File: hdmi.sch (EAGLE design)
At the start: 146 parts, among them IC1 FT2232HQ, U0 6SLX45CSG324, U1 MT41J64M16, U2 TPD12S016RKTR, U3 TPD12S016RKTR, U4 TPD12S016RKTR, U5 MNR18, U6 MNR18, U8 20Mhz

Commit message: +Bluetooth module
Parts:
- added C64, C65: 0.1, prj-hdmi:C-EU0402
- added R42, R47: 10k, prj-hdmi:R-EU_0402
- added U$11: PAN1322, prj-hdmi:PAN1322
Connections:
- new net BT_CTS: U$11.P0.7_UARTCTS, U0B2.IO_L63N_2
- new net BT_RESET#: R42.2, U$11.RESET#, U0B2.IO_L48N_RDWR_B_VREF_2
- new net BT_RTS: U$11.P0.6_UARTRTS, U0B2.IO_L63P_2
- new net BT_RX: U$11.P0.5_UARTRXD, U0B2.IO_L62N_D6_2
- new net BT_SCL: U$11.P0.13_SCL0, U0B2.IO_L49N_D4_2
- new net BT_SDA: U$11.P0.12_SDA0, U0B2.IO_L49P_D3_2
- new net BT_TX: U$11.P0.4_UARTTXD, U0B2.IO_L62P_D5_2
- new net BT_WAKE: R47.1, U$11.P0.14_LPMIN, U0B2.IO_L48P_D7_2
- net +3V3: now also C64.1, C65.1, R47.2, U$11.ONOFF, U$11.VDD1, U$11.VDDUART, U$11.VSUPPLY@A4, U$11.VSUPPLY@A5, U$11.VSUPPLY@A6
- net GND: now also C64.2, C65.2, R42.1, U$11.VSS@A1, U$11.VSS@A11, U$11.VSS@A12, U$11.VSS@A7, U$11.VSS@A9, U$11.VSS@C8, U$11.VSS@C9, U$11.VSS@D7, U$11.VSS@D8, U$11.VSS@E8, U$11.VSS@E9, U$11.VSS@F1, U$11.VSS@F11, U$11.VSS@F12, U$11.VSS@F9

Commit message: Began moving components in the board layout
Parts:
- JP1: device prj-hdmi:JP2W -> prj-hdmi:JP2E
- U$10: device Texas Instruments:TPD4S014SON -> prj-hdmi:TPD4S014SON
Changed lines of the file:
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@@
 <clearance class="2" value="0.127"/>
 </class>
+<class number="3" name="ddr3_vref" width="0.508" drill="0">
+<clearance class="3" value="0.508"/>
+</class>
 </classes>
 <parts>
@@
 <part name="GND32" library="supply1" deviceset="GND" device=""/>
 <part name="GND33" library="supply1" deviceset="GND" device=""/>
-<part name="U$10" library="Texas Instruments" deviceset="TPD4S014" device="SON"/>
+<part name="U$10" library="prj-hdmi" deviceset="TPD4S014" device="SON"/>
 <part name="GND48" library="supply1" deviceset="GND" device=""/>
 <part name="R44" library="resistor" deviceset="R-EU_" device="R0402" value="10k"/>
@@
 <part name="+3V13" library="supply1" deviceset="+3V3" device=""/>
 <part name="GND51" library="supply1" deviceset="GND" device=""/>
-<part name="JP1" library="prj-hdmi" deviceset="JP2W" device="" value="5V_SEL"/>
+<part name="JP1" library="prj-hdmi" deviceset="JP2E" device="" value="5V_SEL"/>
 <part name="GND53" library="supply1" deviceset="GND" device=""/>
 <part name="SV3" library="prj-hdmi" deviceset="MA02-1" device="" value="EXT_SUP"/>
@@
 </segment>
 </net>
-<net name="+1V5_VREF" class="0">
+<net name="+1V5_VREF" class="3">
 <segment>
 <pinref part="U0" gate="B3" pin="IO_L1N_VREF_3"/>

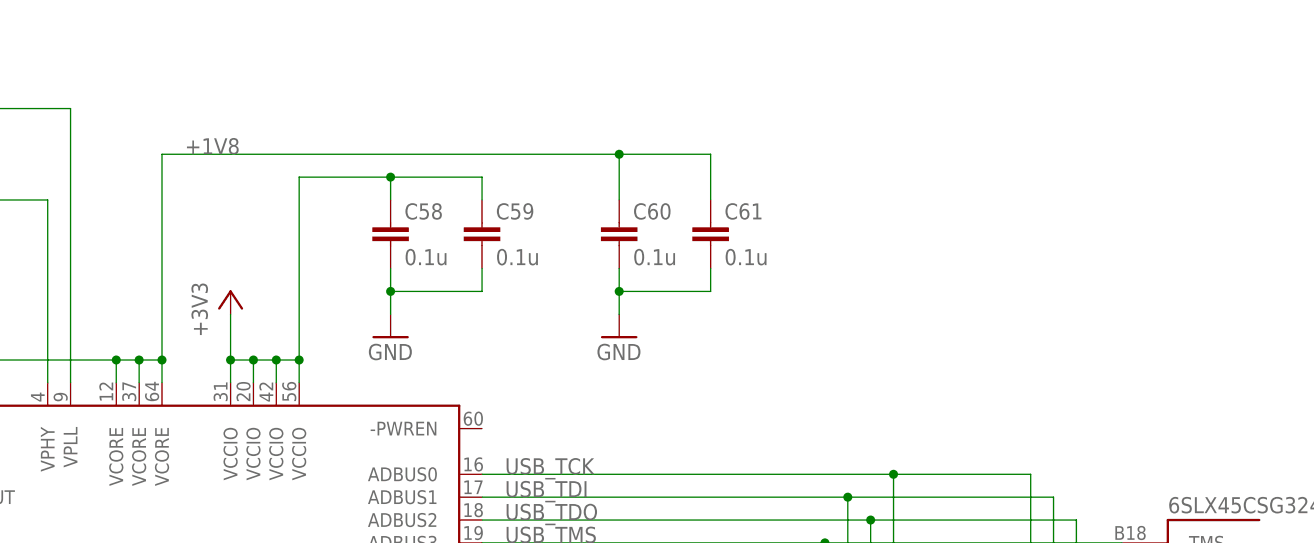
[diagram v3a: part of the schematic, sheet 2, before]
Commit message: Rerouted USB, added more bypass capacitors at the FT2232H
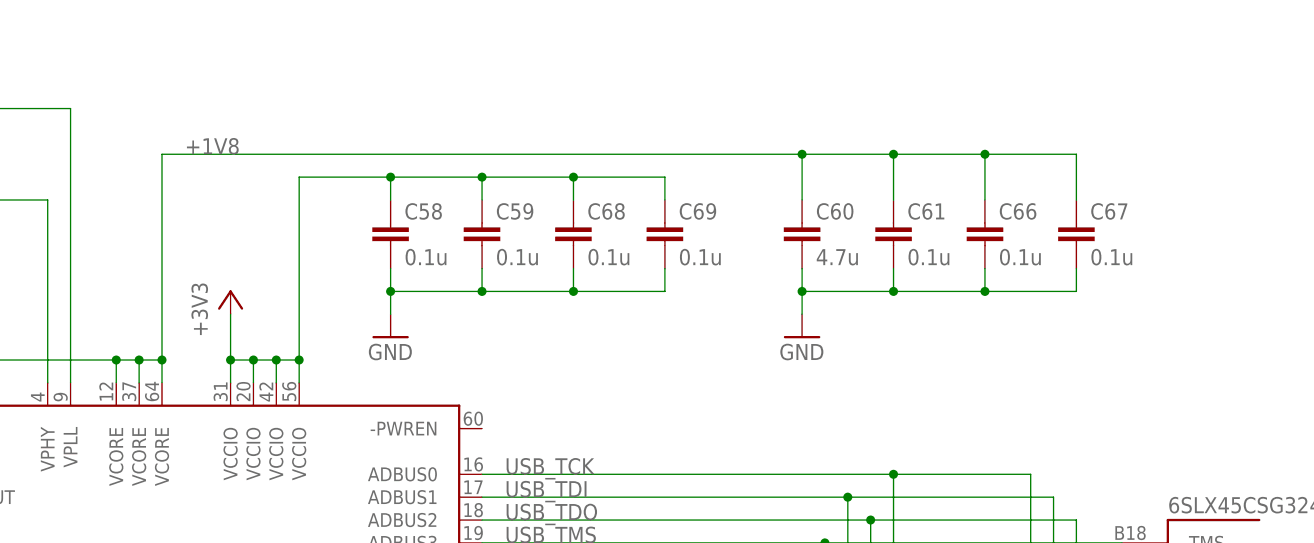
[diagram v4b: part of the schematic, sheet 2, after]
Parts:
- added C66, C67, C68, C69: 0.1u, resistor:C-EUC0402
- C60: value 0.1u -> 4.7u
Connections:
- net +1V8: now also C66.1, C67.1
- net +3V3: now also C68.1, C69.1
- net GND: now also C66.2, C67.2, C68.2, C69.2
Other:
- moved on the sheet: C60, C61
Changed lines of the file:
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@@
 <part name="+3V10" library="supply1" deviceset="+3V3" device=""/>
 <part name="GND39" library="supply1" deviceset="GND" device=""/>
-<part name="C60" library="resistor" deviceset="C-EU" device="C0402" value="0.1u"/>
+<part name="C60" library="resistor" deviceset="C-EU" device="C0402" value="4.7u"/>
 <part name="C61" library="resistor" deviceset="C-EU" device="C0402" value="0.1u"/>
 <part name="R27" library="resistor" deviceset="R-EU_" device="R0402" value="1k"/>
@@
 <part name="R47" library="prj-hdmi" deviceset="R-EU_" device="0402" value="10k"/>
 <part name="+3V21" library="prj-hdmi" deviceset="+3V3" device=""/>
+<part name="C66" library="resistor" deviceset="C-EU" device="C0402" value="0.1u"/>
+<part name="C67" library="resistor" deviceset="C-EU" device="C0402" value="0.1u"/>
+<part name="C68" library="resistor" deviceset="C-EU" device="C0402" value="0.1u"/>
+<part name="C69" library="resistor" deviceset="C-EU" device="C0402" value="0.1u"/>
 </parts>
 <sheets>
@@
 <instance part="+3V10" gate="G$1" x="243.84" y="154.94"/>
 <instance part="GND39" gate="1" x="261.62" y="149.86"/>
-<instance part="C60" gate="G$1" x="287.02" y="162.56"/>
-<instance part="C61" gate="G$1" x="297.18" y="162.56"/>
+<instance part="C60" gate="G$1" x="307.34" y="162.56"/>
+<instance part="C61" gate="G$1" x="317.5" y="162.56"/>
 <instance part="GND41" gate="1" x="340.36" y="111.76"/>
-<instance part="GND33" gate="1" x="287.02" y="149.86"/>
+<instance part="GND33" gate="1" x="307.34" y="149.86"/>
 <instance part="U$10" gate="G$1" x="93.98" y="121.92"/>
 <instance part="GND48" gate="1" x="129.54" y="106.68"/>
@@
 <instance part="+3V13" gate="G$1" x="325.12" y="111.76"/>
 <instance part="GND51" gate="1" x="317.5" y="99.06"/>
+<instance part="C66" gate="G$1" x="327.66" y="162.56"/>
+<instance part="C67" gate="G$1" x="337.82" y="162.56"/>
+<instance part="C68" gate="G$1" x="281.94" y="162.56"/>
+<instance part="C69" gate="G$1" x="292.1" y="162.56"/>
 </instances>
 <busses>
@@
 <wire x1="261.62" y1="157.48" x2="261.62" y2="154.94" width="0.1524" layer="91"/>
 <junction x="261.62" y="154.94"/>
+<pinref part="C68" gate="G$1" pin="2"/>
+<wire x1="271.78" y1="154.94" x2="281.94" y2="154.94" width="0.1524" layer="91"/>
+<wire x1="281.94" y1="154.94" x2="281.94" y2="157.48" width="0.1524" layer="91"/>
+<junction x="271.78" y="154.94"/>
+<pinref part="C69" gate="G$1" pin="2"/>
+<wire x1="281.94" y1="154.94" x2="292.1" y2="154.94" width="0.1524" layer="91"/>
+<wire x1="292.1" y1="154.94" x2="292.1" y2="157.48" width="0.1524" layer="91"/>
+<junction x="281.94" y="154.94"/>
 </segment>
 <segment>
 <pinref part="C60" gate="G$1" pin="2"/>
-<wire x1="287.02" y1="157.48" x2="287.02" y2="154.94" width="0.1524" layer="91"/>
+<wire x1="307.34" y1="157.48" x2="307.34" y2="154.94" width="0.1524" layer="91"/>
 <pinref part="C61" gate="G$1" pin="2"/>
-<wire x1="297.18" y1="157.48" x2="297.18" y2="154.94" width="0.1524" layer="91"/>
-<wire x1="297.18" y1="154.94" x2="287.02" y2="154.94" width="0.1524" layer="91"/>
+<wire x1="317.5" y1="157.48" x2="317.5" y2="154.94" width="0.1524" layer="91"/>
+<wire x1="317.5" y1="154.94" x2="307.34" y2="154.94" width="0.1524" layer="91"/>
 <pinref part="GND33" gate="1" pin="GND"/>
-<wire x1="287.02" y1="152.4" x2="287.02" y2="154.94" width="0.1524" layer="91"/>
-<junction x="287.02" y="154.94"/>
+<wire x1="307.34" y1="152.4" x2="307.34" y2="154.94" width="0.1524" layer="91"/>
+<junction x="307.34" y="154.94"/>
+<pinref part="C66" gate="G$1" pin="2"/>
+<wire x1="317.5" y1="154.94" x2="327.66" y2="154.94" width="0.1524" layer="91"/>
+<wire x1="327.66" y1="154.94" x2="327.66" y2="157.48" width="0.1524" layer="91"/>
+<junction x="317.5" y="154.94"/>
+<pinref part="C67" gate="G$1" pin="2"/>
+<wire x1="327.66" y1="154.94" x2="337.82" y2="154.94" width="0.1524" layer="91"/>
+<wire x1="337.82" y1="154.94" x2="337.82" y2="157.48" width="0.1524" layer="91"/>
+<junction x="327.66" y="154.94"/>
 </segment>
 <segment>
@@
 <pinref part="C59" gate="G$1" pin="1"/>
 <wire x1="271.78" y1="167.64" x2="271.78" y2="165.1" width="0.1524" layer="91"/>
+<pinref part="C68" gate="G$1" pin="1"/>
+<wire x1="271.78" y1="167.64" x2="281.94" y2="167.64" width="0.1524" layer="91"/>
+<wire x1="281.94" y1="167.64" x2="281.94" y2="165.1" width="0.1524" layer="91"/>
+<junction x="271.78" y="167.64"/>
+<pinref part="C69" gate="G$1" pin="1"/>
+<wire x1="281.94" y1="167.64" x2="292.1" y2="167.64" width="0.1524" layer="91"/>
+<wire x1="292.1" y1="167.64" x2="292.1" y2="165.1" width="0.1524" layer="91"/>
+<junction x="281.94" y="167.64"/>
 </segment>
 <segment>
@@
 <junction x="231.14" y="147.32"/>
 <wire x1="236.22" y1="147.32" x2="236.22" y2="170.18" width="0.1524" layer="91"/>
-<wire x1="236.22" y1="170.18" x2="287.02" y2="170.18" width="0.1524" layer="91"/>
+<wire x1="236.22" y1="170.18" x2="307.34" y2="170.18" width="0.1524" layer="91"/>
 <junction x="236.22" y="147.32"/>
 <pinref part="C60" gate="G$1" pin="1"/>
-<wire x1="287.02" y1="170.18" x2="287.02" y2="165.1" width="0.1524" layer="91"/>
+<wire x1="307.34" y1="170.18" x2="307.34" y2="165.1" width="0.1524" layer="91"/>
 <pinref part="C61" gate="G$1" pin="1"/>
-<wire x1="287.02" y1="170.18" x2="297.18" y2="170.18" width="0.1524" layer="91"/>
-<wire x1="297.18" y1="170.18" x2="297.18" y2="165.1" width="0.1524" layer="91"/>
-<junction x="287.02" y="170.18"/>
+<wire x1="307.34" y1="170.18" x2="317.5" y2="170.18" width="0.1524" layer="91"/>
+<wire x1="317.5" y1="170.18" x2="317.5" y2="165.1" width="0.1524" layer="91"/>
+<junction x="307.34" y="170.18"/>
 <label x="238.76" y="170.18" size="1.778" layer="95"/>
-</segment>
-</net>
+<pinref part="C66" gate="G$1" pin="1"/>
+<wire x1="317.5" y1="170.18" x2="327.66" y2="170.18" width="0.1524" layer="91"/>
+<wire x1="327.66" y1="170.18" x2="327.66" y2="165.1" width="0.1524" layer="91"/>
+<junction x="317.5" y="170.18"/>
+<pinref part="C67" gate="G$1" pin="1"/>
+<wire x1="327.66" y1="170.18" x2="337.82" y2="170.18" width="0.1524" layer="91"/>
+<wire x1="337.82" y1="170.18" x2="337.82" y2="165.1" width="0.1524" layer="91"/>
+<junction x="327.66" y="170.18"/>
+</segment>
+</net>
